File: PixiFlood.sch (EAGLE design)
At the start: 31 parts, among them IC1 TC7W04FP-0.65, IC2 WS2811SOP8, IC3 78L05Z, U1 PT4115B89E, U2 PT4115B89E, U3 PT4115B89E, X1 22-23-2031, X2 22-23-2031

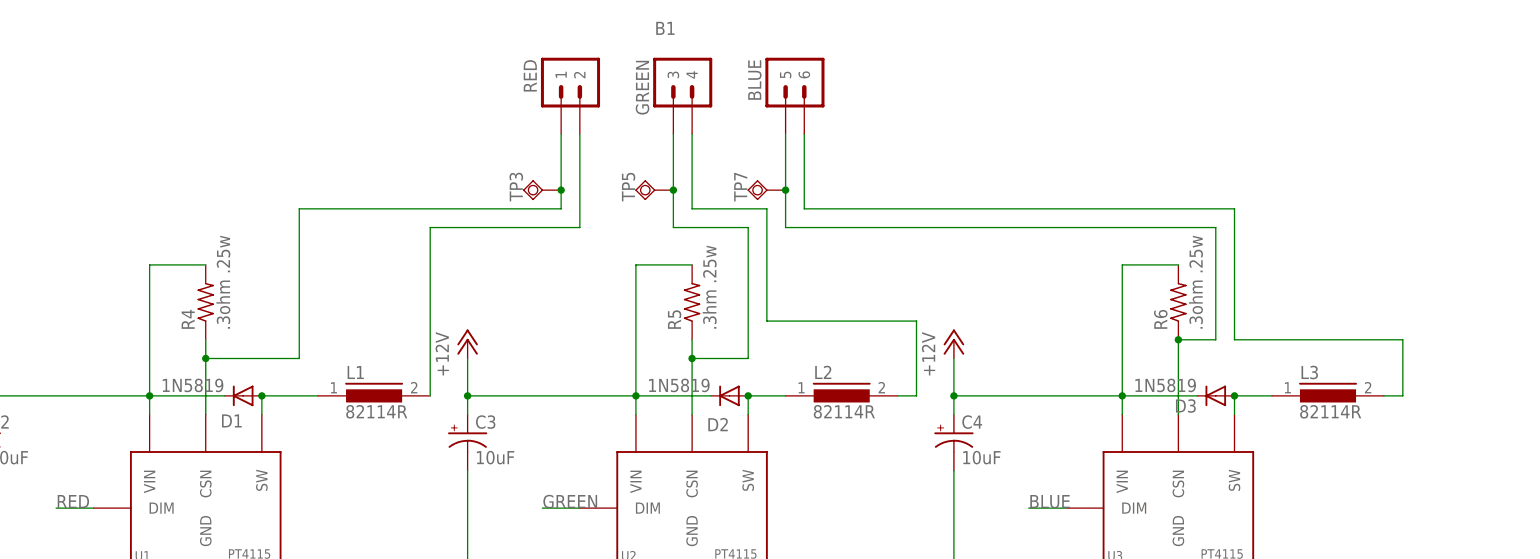
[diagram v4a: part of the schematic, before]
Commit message: Reworked layout
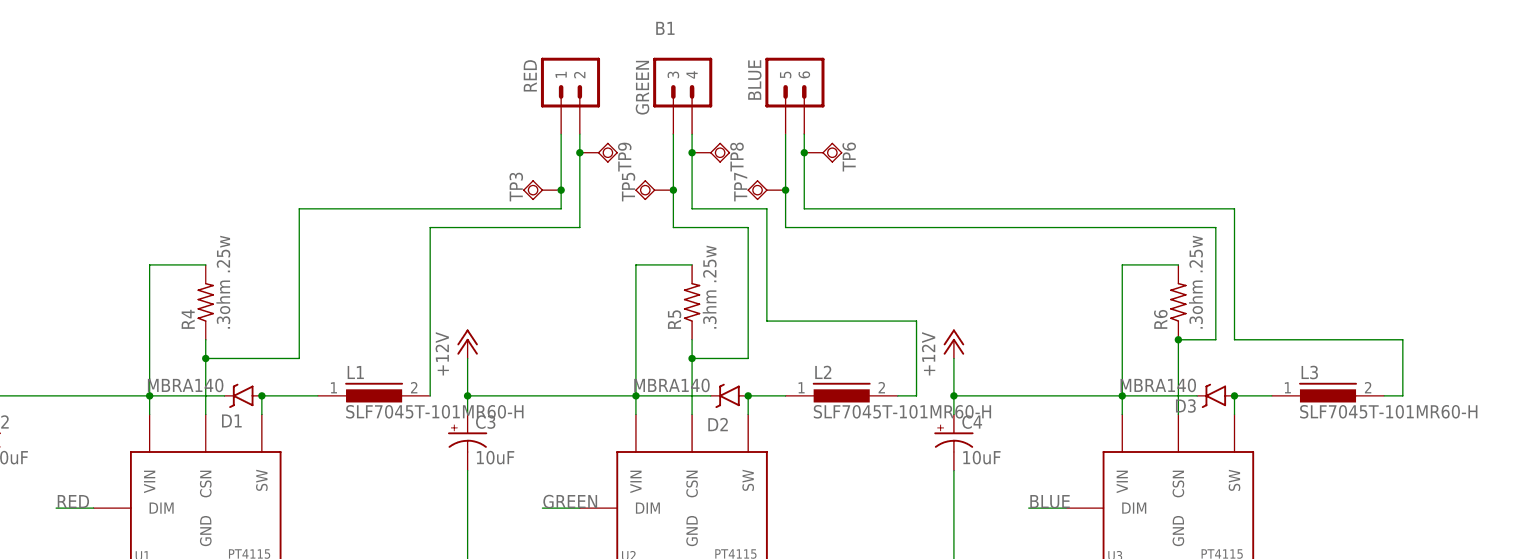
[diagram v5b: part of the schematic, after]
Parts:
- added TP6, TP8, TP9: TPSQTP15SQ, testpad:TPSQTP15SQ
- C1: device capacitors:CAP_POLPTH50 -> capacitors:CAP_POL1206
- C2, C3, C4: device adafruit:CPOL-USE2.5-5 -> capacitors:CAP_POLCASE_D
- D1, D2, D3: value 1N5819 -> MBRA140; device diode:DIODE-DO07 -> SparkFun-DiscreteSemi:DIODE-SCHOTTKY-MBRA140
- L1, L2, L3: value 82114R -> SLF7045T-101MR60-H; device inductors:82114R -> inductors:SLF7045
- R1, R2, R3: device rcl:R-US_0204/5 -> rcl:R-US_M1206
- R4, R5, R6: device resistor:R-US_0204/5 -> resistor:R-US_R1210
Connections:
- net N$10: now also TP6.TP
- net N$3: now also TP9.TP
- net N$9: now also TP8.TP
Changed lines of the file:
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@@
 <part name="U2" library="drivers" deviceset="PT4115" device="B89E"/>
 <part name="U3" library="drivers" deviceset="PT4115" device="B89E"/>
-<part name="D1" library="diode" deviceset="DIODE-" device="DO07" value="1N5819"/>
-<part name="D2" library="diode" deviceset="DIODE-" device="DO07" value="1N5819"/>
-<part name="D3" library="diode" deviceset="DIODE-" device="DO07" value="1N5819"/>
-<part name="R4" library="resistor" deviceset="R-US_" device="0204/5" value=".3ohm .25w"/>
-<part name="R5" library="resistor" deviceset="R-US_" device="0204/5" value=".3hm .25w"/>
-<part name="R6" library="resistor" deviceset="R-US_" device="0204/5" value=".3ohm .25w"/>
+<part name="D1" library="SparkFun-DiscreteSemi" deviceset="DIODE-SCHOTTKY" device="-MBRA140" value="MBRA140"/>
+<part name="D2" library="SparkFun-DiscreteSemi" deviceset="DIODE-SCHOTTKY" device="-MBRA140" value="MBRA140"/>
+<part name="D3" library="SparkFun-DiscreteSemi" deviceset="DIODE-SCHOTTKY" device="-MBRA140" value="MBRA140"/>
+<part name="R4" library="resistor" deviceset="R-US_" device="R1210" value=".3ohm .25w"/>
+<part name="R5" library="resistor" deviceset="R-US_" device="R1210" value=".3hm .25w"/>
+<part name="R6" library="resistor" deviceset="R-US_" device="R1210" value=".3ohm .25w"/>
 <part name="P+5" library="supply1" deviceset="+12V" device=""/>
 <part name="GND5" library="supply1" deviceset="GND" device=""/>
 <part name="GND6" library="supply1" deviceset="GND" device=""/>
 <part name="GND7" library="supply1" deviceset="GND" device=""/>
-<part name="L3" library="inductors" deviceset="82114R" device=""/>
-<part name="L2" library="inductors" deviceset="82114R" device=""/>
-<part name="L1" library="inductors" deviceset="82114R" device=""/>
+<part name="L3" library="inductors" deviceset="SLF7045" device="" value="SLF7045T-101MR60-H"/>
+<part name="L2" library="inductors" deviceset="SLF7045" device="" value="SLF7045T-101MR60-H"/>
+<part name="L1" library="inductors" deviceset="SLF7045" device="" value="SLF7045T-101MR60-H"/>
 <part name="GND4" library="supply1" deviceset="GND" device=""/>
 <part name="IC3" library="linear" deviceset="78*" device="Z" technology="L05"/>
 <part name="P+3" library="supply1" deviceset="+12V" device=""/>
 <part name="P+4" library="supply1" deviceset="+5V" device=""/>
-<part name="R3" library="rcl" deviceset="R-US_" device="0204/5" value="100ohm"/>
+<part name="R3" library="rcl" deviceset="R-US_" device="M1206" value="100ohm"/>
 <part name="IC2" library="drivers" deviceset="WS2811" device="SOP8"/>
 <part name="X1" library="MyLibrary" deviceset="22-23-2031" device=""/>
 <part name="X2" library="MyLibrary" deviceset="22-23-2031" device=""/>
-<part name="R2" library="rcl" deviceset="R-US_" device="0204/5" value="33R"/>
-<part name="R1" library="rcl" deviceset="R-US_" device="0204/5" value="33R"/>
+<part name="R2" library="rcl" deviceset="R-US_" device="M1206" value="33R"/>
+<part name="R1" library="rcl" deviceset="R-US_" device="M1206" value="33R"/>
 <part name="P+1" library="supply1" deviceset="+12V" device=""/>
 <part name="P+2" library="supply1" deviceset="+12V" device=""/>
@@
 <part name="TP1" library="testpad" deviceset="TPSQ" device="TP20R"/>
 <part name="TP2" library="testpad" deviceset="TPSQ" device="TP20SQ" value="TPSQTP20SQ"/>
-<part name="C1" library="capacitors" deviceset="CAP_POL" device="PTH50" value=".1uF"/>
+<part name="C1" library="capacitors" deviceset="CAP_POL" device="1206" value=".1uF"/>
 <part name="P+6" library="supply1" deviceset="+12V" device=""/>
 <part name="P+7" library="supply1" deviceset="+12V" device=""/>
 <part name="B1" library="special" deviceset="LED-BOARD" device="V2"/>
-<part name="C2" library="adafruit" deviceset="CPOL-US" device="E2.5-5" value="10uF"/>
-<part name="C3" library="adafruit" deviceset="CPOL-US" device="E2.5-5" value="10uF"/>
-<part name="C4" library="adafruit" deviceset="CPOL-US" device="E2.5-5" value="10uF"/>
+<part name="C2" library="capacitors" deviceset="CAP_POL" device="CASE_D" value="10uF"/>
+<part name="C3" library="capacitors" deviceset="CAP_POL" device="CASE_D" value="10uF"/>
+<part name="C4" library="capacitors" deviceset="CAP_POL" device="CASE_D" value="10uF"/>
 <part name="TP3" library="testpad" deviceset="TPSQ" device="TP15R" value="TPSQTP15R"/>
 <part name="TP5" library="testpad" deviceset="TPSQ" device="TP15R" value="TPSQTP15R"/>
 <part name="TP7" library="testpad" deviceset="TPSQ" device="TP15R" value="TPSQTP15R"/>
+<part name="TP6" library="testpad" deviceset="TPSQ" device="TP15SQ"/>
+<part name="TP8" library="testpad" deviceset="TPSQ" device="TP15SQ"/>
+<part name="TP9" library="testpad" deviceset="TPSQ" device="TP15SQ"/>
 </parts>
 <sheets>
@@
 <instance part="GND6" gate="1" x="-66.04" y="-132.08"/>
 <instance part="GND7" gate="1" x="0" y="-132.08"/>
-<instance part="L3" gate="1" x="20.32" y="-99.06"/>
-<instance part="L2" gate="1" x="-45.72" y="-99.06"/>
-<instance part="L1" gate="1" x="-109.22" y="-99.06"/>
+<instance part="L3" gate="G$1" x="20.32" y="-99.06"/>
+<instance part="L2" gate="G$1" x="-45.72" y="-99.06"/>
+<instance part="L1" gate="G$1" x="-109.22" y="-99.06"/>
 <instance part="GND4" gate="1" x="-72.39" y="-33.02"/>
 <instance part="IC3" gate="A1" x="-96.52" y="-20.32"/>
@@
 <instance part="TP5" gate="G$1" x="-71.12" y="-71.12" rot="R270"/>
 <instance part="TP7" gate="G$1" x="-55.88" y="-71.12" rot="R270"/>
+<instance part="TP6" gate="G$1" x="-48.26" y="-66.04" rot="R90"/>
+<instance part="TP8" gate="G$1" x="-63.5" y="-66.04" rot="R90"/>
+<instance part="TP9" gate="G$1" x="-78.74" y="-66.04" rot="R90"/>
 </instances>
 <busses>
@@
 <pinref part="U3" gate="IC" pin="SW"/>
 <pinref part="D3" gate="G$1" pin="A"/>
-<pinref part="L3" gate="1" pin="1"/>
+<pinref part="L3" gate="G$1" pin="1"/>
 <wire x1="12.7" y1="-99.06" x2="7.62" y2="-99.06" width="0.1524" layer="91"/>
 <wire x1="7.62" y1="-101.6" x2="7.62" y2="-99.06" width="0.1524" layer="91"/>
@@
 <pinref part="U2" gate="IC" pin="SW"/>
 <pinref part="D2" gate="G$1" pin="A"/>
-<pinref part="L2" gate="1" pin="1"/>
+<pinref part="L2" gate="G$1" pin="1"/>
 <wire x1="-53.34" y1="-99.06" x2="-58.42" y2="-99.06" width="0.1524" layer="91"/>
 <wire x1="-58.42" y1="-101.6" x2="-58.42" y2="-99.06" width="0.1524" layer="91"/>
@@
 <pinref part="U1" gate="IC" pin="SW"/>
 <pinref part="D1" gate="G$1" pin="A"/>
-<pinref part="L1" gate="1" pin="1"/>
+<pinref part="L1" gate="G$1" pin="1"/>
 <wire x1="-116.84" y1="-99.06" x2="-124.46" y2="-99.06" width="0.1524" layer="91"/>
 <wire x1="-124.46" y1="-101.6" x2="-124.46" y2="-99.06" width="0.1524" layer="91"/>
@@
 <net name="N$3" class="0">
 <segment>
-<pinref part="L1" gate="1" pin="2"/>
+<pinref part="L1" gate="G$1" pin="2"/>
 <wire x1="-101.6" y1="-99.06" x2="-101.6" y2="-76.2" width="0.1524" layer="91"/>
 <pinref part="B1" gate="G$1" pin="2"/>
 <wire x1="-101.6" y1="-76.2" x2="-81.28" y2="-76.2" width="0.1524" layer="91"/>
-<wire x1="-81.28" y1="-76.2" x2="-81.28" y2="-63.5" width="0.1524" layer="91"/>
+<wire x1="-81.28" y1="-76.2" x2="-81.28" y2="-66.04" width="0.1524" layer="91"/>
+<pinref part="TP9" gate="G$1" pin="TP"/>
+<wire x1="-81.28" y1="-66.04" x2="-81.28" y2="-63.5" width="0.1524" layer="91"/>
+<junction x="-81.28" y="-66.04"/>
 </segment>
 </net>
 <net name="N$9" class="0">
 <segment>
-<pinref part="L2" gate="1" pin="2"/>
+<pinref part="L2" gate="G$1" pin="2"/>
 <wire x1="-35.56" y1="-99.06" x2="-38.1" y2="-99.06" width="0.1524" layer="91"/>
 <wire x1="-35.56" y1="-99.06" x2="-35.56" y2="-88.9" width="0.1524" layer="91"/>
@@
 <pinref part="B1" gate="G$1" pin="4"/>
 <wire x1="-55.88" y1="-73.66" x2="-66.04" y2="-73.66" width="0.1524" layer="91"/>
-<wire x1="-66.04" y1="-73.66" x2="-66.04" y2="-63.5" width="0.1524" layer="91"/>
+<wire x1="-66.04" y1="-73.66" x2="-66.04" y2="-66.04" width="0.1524" layer="91"/>
+<pinref part="TP8" gate="G$1" pin="TP"/>
+<wire x1="-66.04" y1="-66.04" x2="-66.04" y2="-63.5" width="0.1524" layer="91"/>
+<junction x="-66.04" y="-66.04"/>
 </segment>
 </net>
 <net name="N$10" class="0">
 <segment>
-<pinref part="L3" gate="1" pin="2"/>
+<pinref part="L3" gate="G$1" pin="2"/>
 <wire x1="30.48" y1="-99.06" x2="27.94" y2="-99.06" width="0.1524" layer="91"/>
 <wire x1="30.48" y1="-99.06" x2="30.48" y2="-91.44" width="0.1524" layer="91"/>
@@
 <pinref part="B1" gate="G$1" pin="6"/>
 <wire x1="7.62" y1="-73.66" x2="-50.8" y2="-73.66" width="0.1524" layer="91"/>
-<wire x1="-50.8" y1="-73.66" x2="-50.8" y2="-63.5" width="0.1524" layer="91"/>
-</segment>
-</net>
+<wire x1="-50.8" y1="-73.66" x2="-50.8" y2="-66.04" width="0.1524" layer="91"/>
+<pinref part="TP6" gate="G$1" pin="TP"/>
+<wire x1="-50.8" y1="-66.04" x2="-50.8" y2="-63.5" width="0.1524" layer="91"/>
+<junction x="-50.8" y="-66.04"/>
+</segment>
+</net>

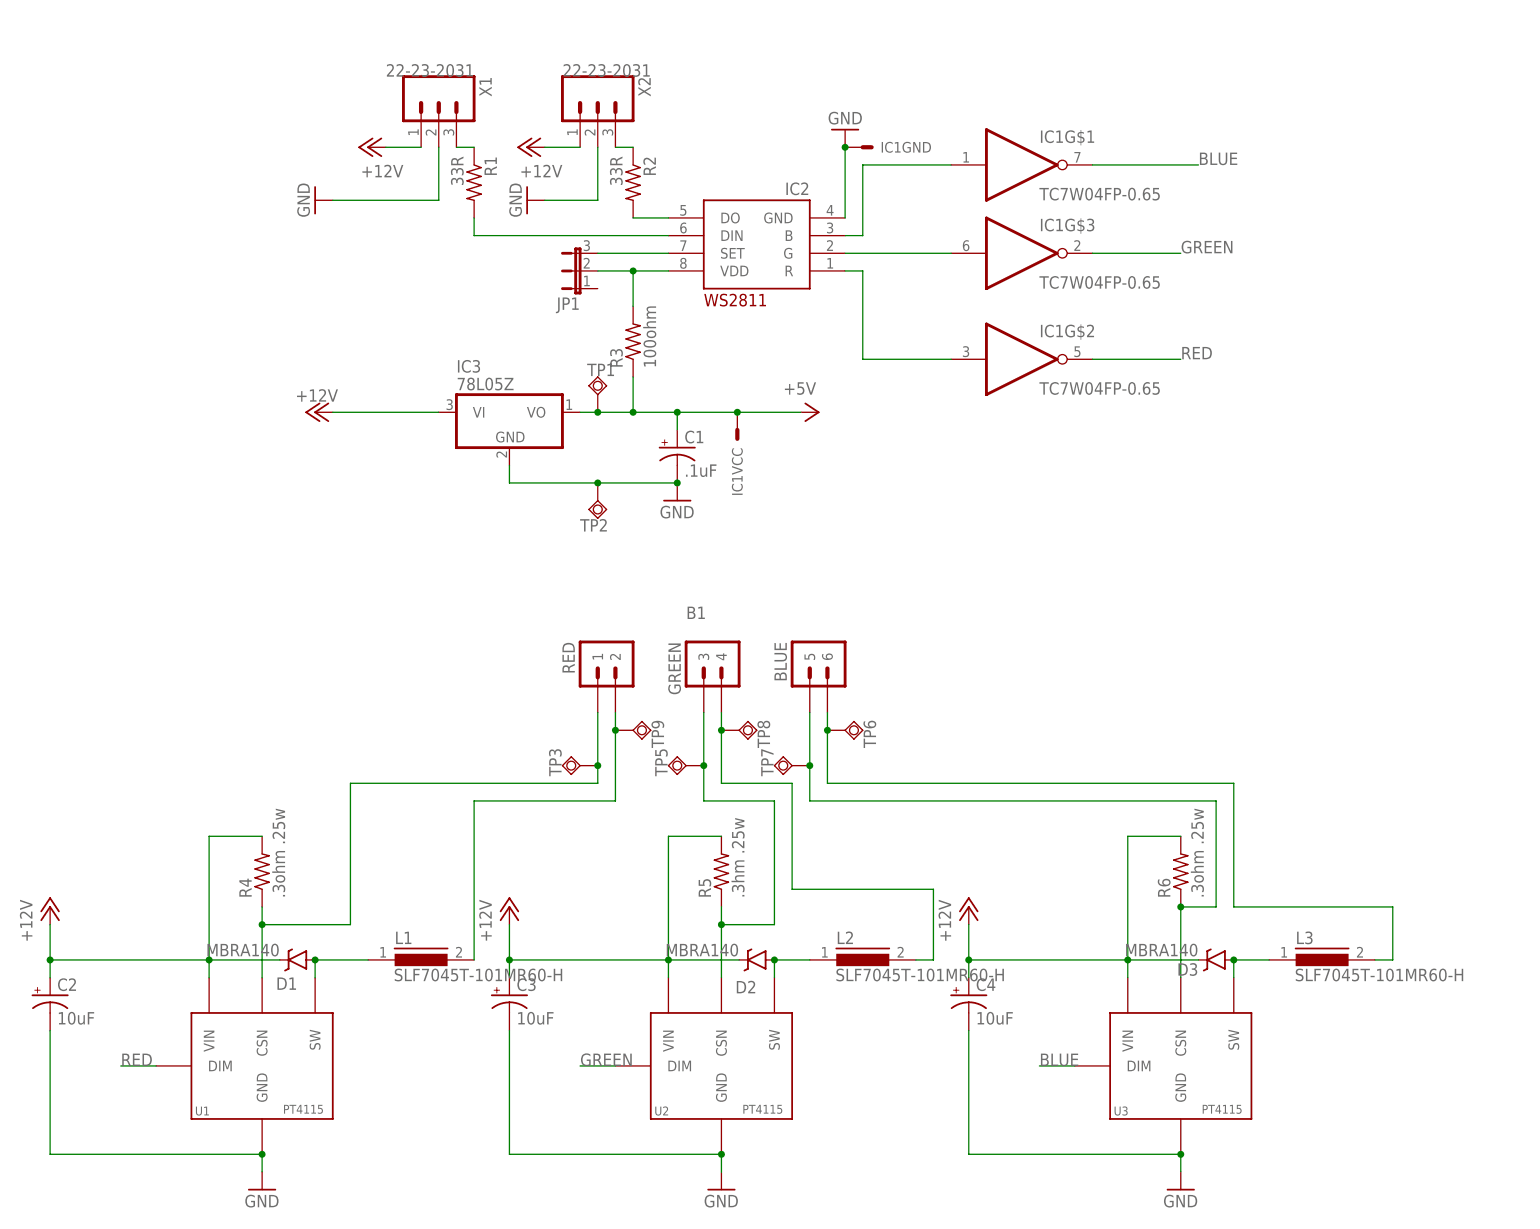
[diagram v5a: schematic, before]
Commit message: Reworked layout
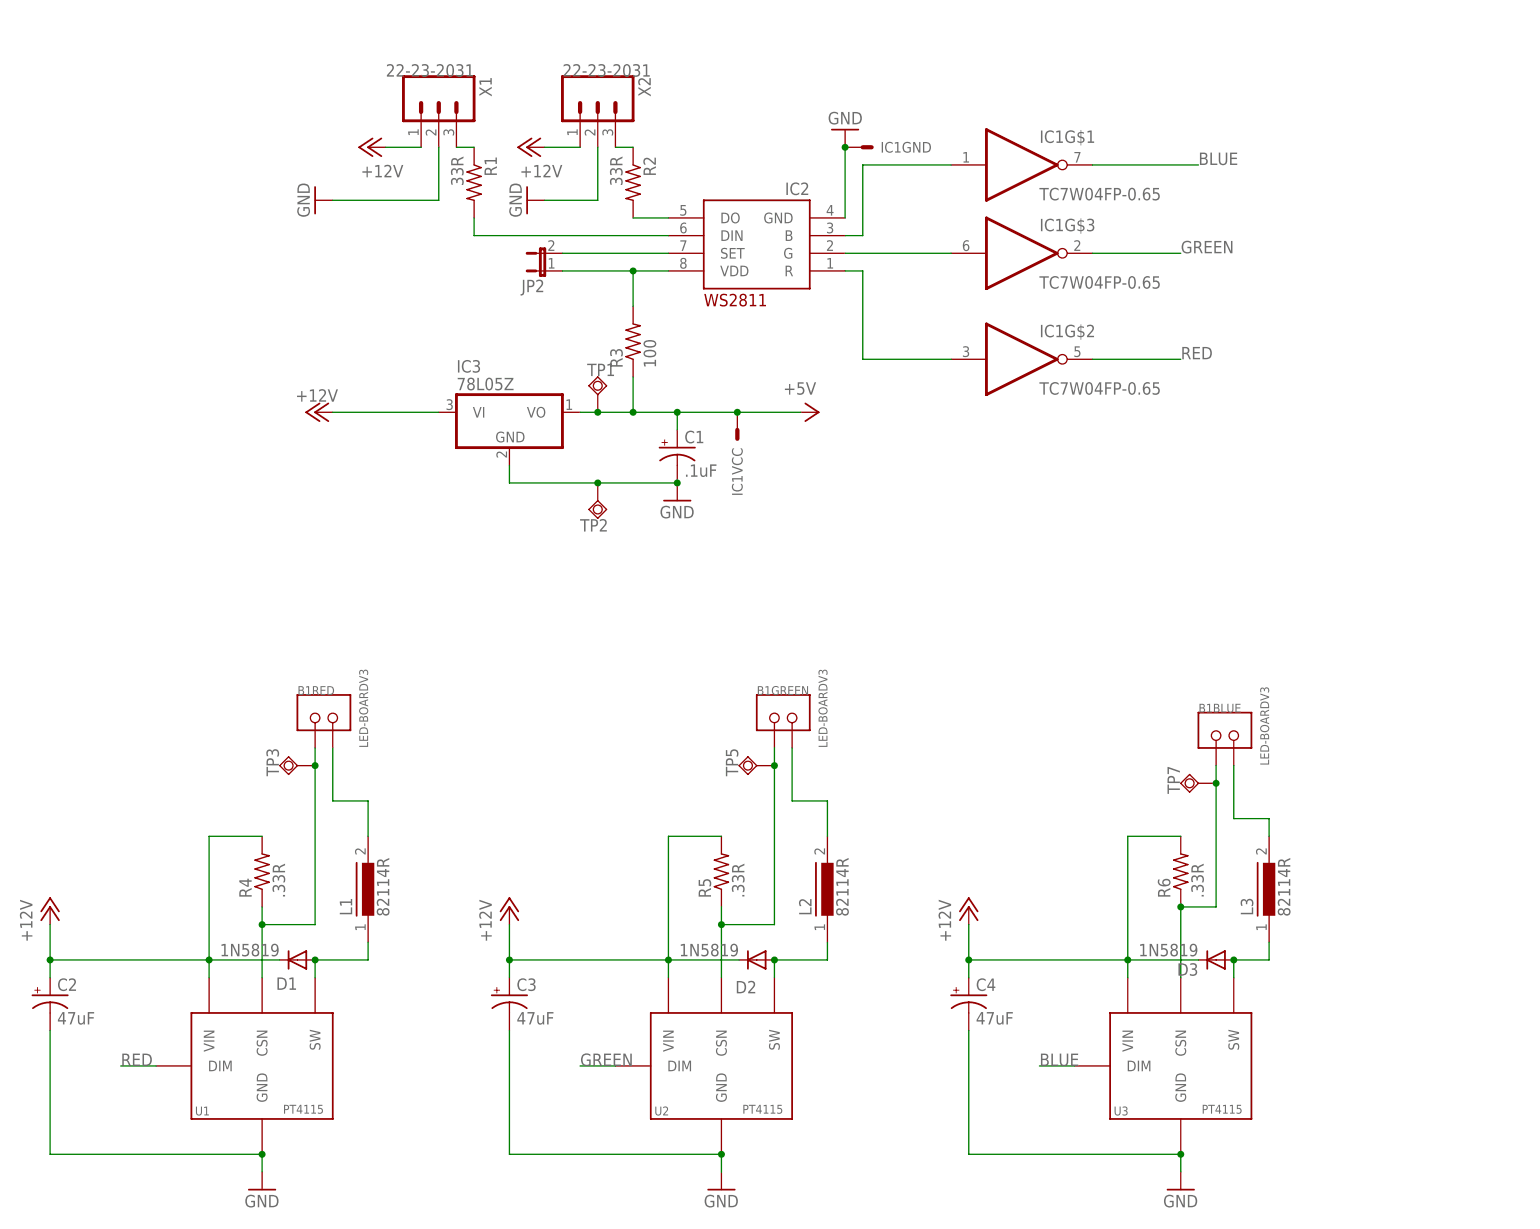
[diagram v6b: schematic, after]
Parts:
- removed JP1: (no value), jumper:JP2E
- removed TP6, TP8, TP9: TPSQTP15SQ, testpad:TPSQTP15SQ
- added JP2: (no value), jumper:JP1E
- B1: value LED-BOARDV2 -> LED-BOARDV3; device special:LED-BOARDV2 -> special:LED-BOARDV3
- C1: device capacitors:CAP_POL1206 -> capacitors:CAP_POLPTH50
- C2, C3, C4: value 10uF -> 47uF; device capacitors:CAP_POLCASE_D -> adafruit:CPOL-USE2.5-5
- D1, D2, D3: value MBRA140 -> 1N5819; device SparkFun-DiscreteSemi:DIODE-SCHOTTKY-MBRA140 -> diode:DIODE-DO07
- L1, L2, L3: value SLF7045T-101MR60-H -> 82114R; device inductors:SLF7045 -> inductors:82114R
- R1, R2: device rcl:R-US_M1206 -> rcl:R-US_0204/7
- R3: value 100ohm -> 100; device rcl:R-US_M1206 -> rcl:R-US_0204/5
- R4, R6: value .3ohm .25w -> .33R; device resistor:R-US_R1210 -> resistor:R-US_0204/7
- R5: value .3hm .25w -> .33R; device resistor:R-US_R1210 -> resistor:R-US_0204/7
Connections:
- removed net N$18: IC2.SET, JP1.3
- new net N$17: IC2.SET, JP2.2
- net BOUT: now also B1BLUE.P$2; no longer B1.5
- net GOUT: now also B1GREEN.P$2; no longer B1.3
- net N$10: now also B1BLUE.P$1; no longer B1.6, TP6.TP
- net N$14: now also JP2.1; no longer JP1.2
- net N$3: now also B1RED.P$1; no longer B1.2, TP9.TP
- net N$9: now also B1GREEN.P$1; no longer B1.4, TP8.TP
- net ROUT: now also B1RED.P$2; no longer B1.1
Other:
- moved on the sheet: TP3, TP5, TP7
